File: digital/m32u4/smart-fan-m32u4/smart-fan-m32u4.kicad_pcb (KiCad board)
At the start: 2 copper layers, 27 parts, among them J1 USB_B_Micro, J2 12V, J5 12V, M1 FAN, Q1 BSS138, Q2 BSS138, Q3 SUD19P06-60, U1 LM2936-5.0, U2 LM2936-3.3, U3 ATmega32U4-MU, U4 MAX31826, Y1 16MHz

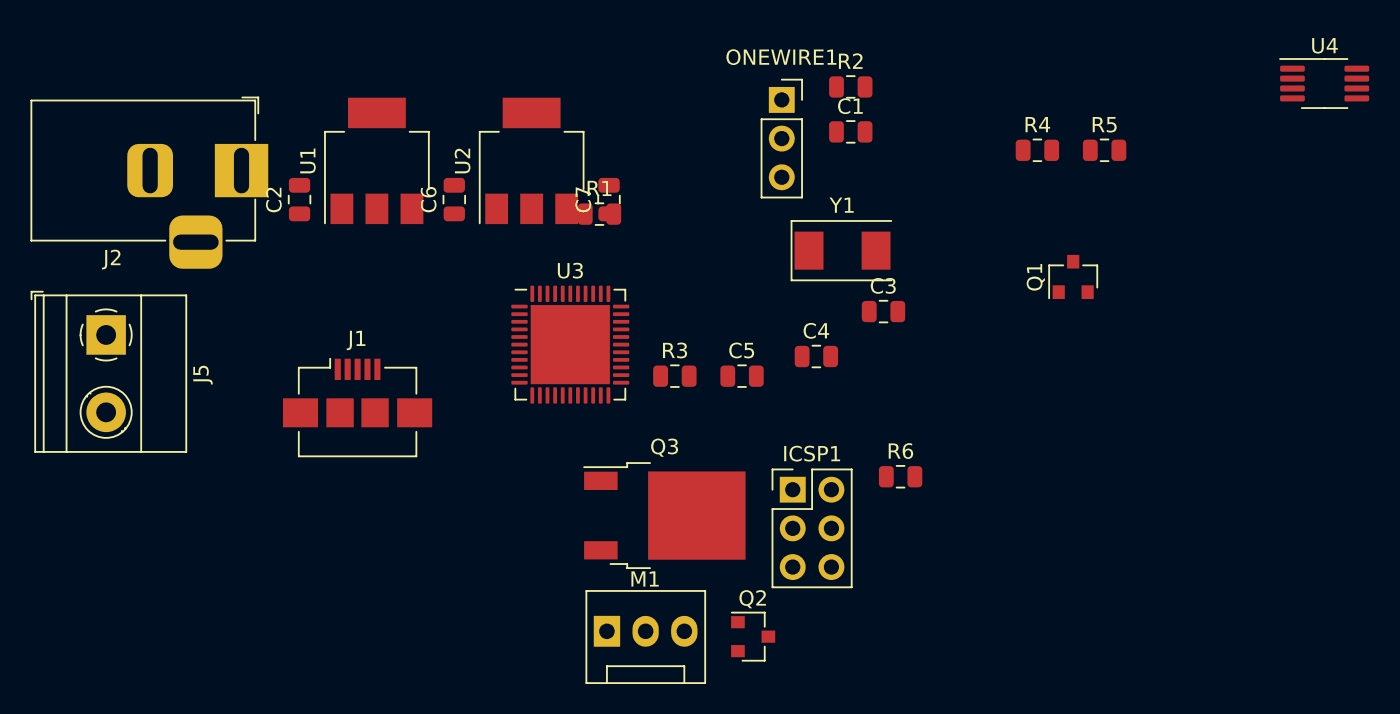
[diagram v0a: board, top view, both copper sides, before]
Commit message: Working on layout and adding 2 more fan channels
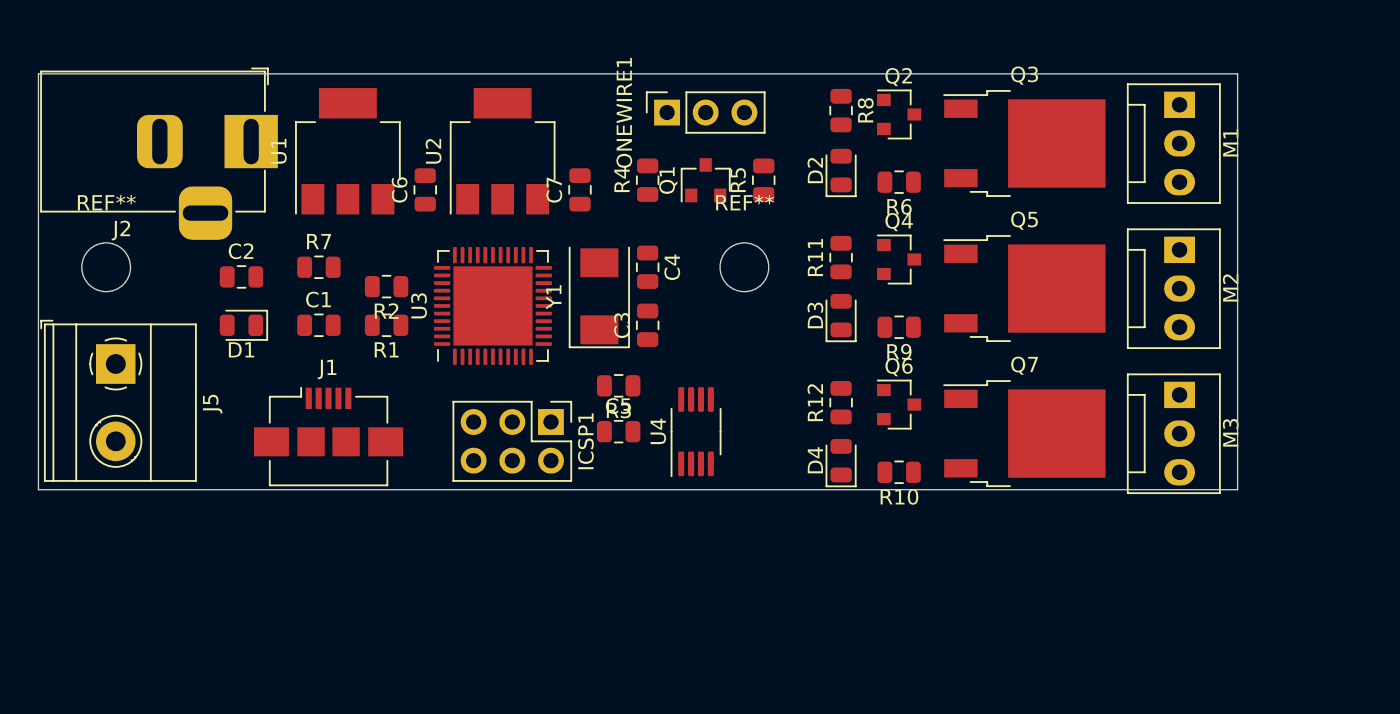
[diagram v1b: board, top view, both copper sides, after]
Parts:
- added D1: GRN_LED, LED_SMD:LED_0805_2012Metric, F.Cu at (114.3, 95.9)
- added D2: RED_LED, LED_SMD:LED_0805_2012Metric, F.Cu at (153.7, 85.7)
- added D3: RED_LED, LED_SMD:LED_0805_2012Metric, F.Cu at (153.7, 95.2)
- added D4: RED_LED, LED_SMD:LED_0805_2012Metric, F.Cu at (153.7, 104.8)
- added M2: FAN2, Connector:FanPinHeader_1x03_P2.54mm_Vertical, F.Cu at (175.9, 90.9)
- added M3: FAN3, Connector:FanPinHeader_1x03_P2.54mm_Vertical, F.Cu at (175.9, 100.5)
- added Q4: BSS138, Package_TO_SOT_SMD:SOT-23, F.Cu at (157.5, 91.6)
- added Q5: SUD19P06-60, Package_TO_SOT_SMD:TO-252-2, F.Cu at (165.7, 93.5)
- added Q6: BSS138, Package_TO_SOT_SMD:SOT-23, F.Cu at (157.5, 101.1)
- added Q7: SUD19P06-60, Package_TO_SOT_SMD:TO-252-2, F.Cu at (165.7, 103.0)
- added R10: 10k, Resistor_SMD:R_0805_2012Metric, F.Cu at (157.5, 105.5)
- added R11: 1k6, Resistor_SMD:R_0805_2012Metric, F.Cu at (153.7, 91.4)
- added R12: 1k6, Resistor_SMD:R_0805_2012Metric, F.Cu at (153.7, 101.0)
- added R7: 5k1, Resistor_SMD:R_0805_2012Metric, F.Cu at (119.4, 92.1)
- added R8: 1k6, Resistor_SMD:R_0805_2012Metric, F.Cu at (153.7, 81.8)
- added R9: 10k, Resistor_SMD:R_0805_2012Metric, F.Cu at (157.5, 96.0)
- added REF**: MountingHole_3.2mm_M3, MountingHole:MountingHole_3.2mm_M3, F.Cu at (147.3, 92.1)
- added REF**: MountingHole_3.2mm_M3, MountingHole:MountingHole_3.2mm_M3, F.Cu at (105.4, 92.1)
- M1: value FAN -> FAN1
- moved M1 51.1 mm to (175.9, 81.4), turned to 270 degrees
- moved U4 47.2 mm to (144.1, 102.9), turned to 90 degrees
- moved C1 37.2 mm to (119.4, 95.9)
- moved Q2 35.6 mm to (157.5, 82.0)
- moved Q3 34.0 mm to (165.7, 83.9)
- moved R2 33.2 mm to (123.8, 93.3), turned to 180 degrees
- moved R4 25.7 mm to (141.0, 86.4), turned to 90 degrees
- moved Q1 25.0 mm to (144.8, 86.4)
- moved R5 22.5 mm to (148.6, 86.4), turned to 90 degrees
- moved R6 19.3 mm to (157.5, 86.5), turned to 180 degrees
- moved ICSP1 16.5 mm to (134.6, 102.2), turned to 270 degrees
- moved Y1 16.2 mm to (137.8, 94.0), turned to 90 degrees
- moved R1 15.8 mm to (123.8, 95.9), turned to 180 degrees
- moved C3 15.5 mm to (141.0, 95.9), turned to 90 degrees
- moved C4 12.5 mm to (141.0, 92.1), turned to 270 degrees
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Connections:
- net FAN_CTRL renamed FAN_CTRL1
- U3 pad 29: Net-(U3-Pad29) -> FAN_CTRL2
- U3 pad 30: Net-(U3-Pad30) -> FAN_CTRL3
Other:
- board outline added: 78.7 x 27.3 mm
